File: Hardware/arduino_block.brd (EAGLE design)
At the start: 30.5 x 62.2 mm, 39 parts, among them U1 MIC5205-3.3V (150mA), U2 EDISON_CONNECTOR_FULLMOUNTING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, U3 EDISON_CONNECTOR_FULLHEADER, U4 ATMEGA328, Y1 8MHZ

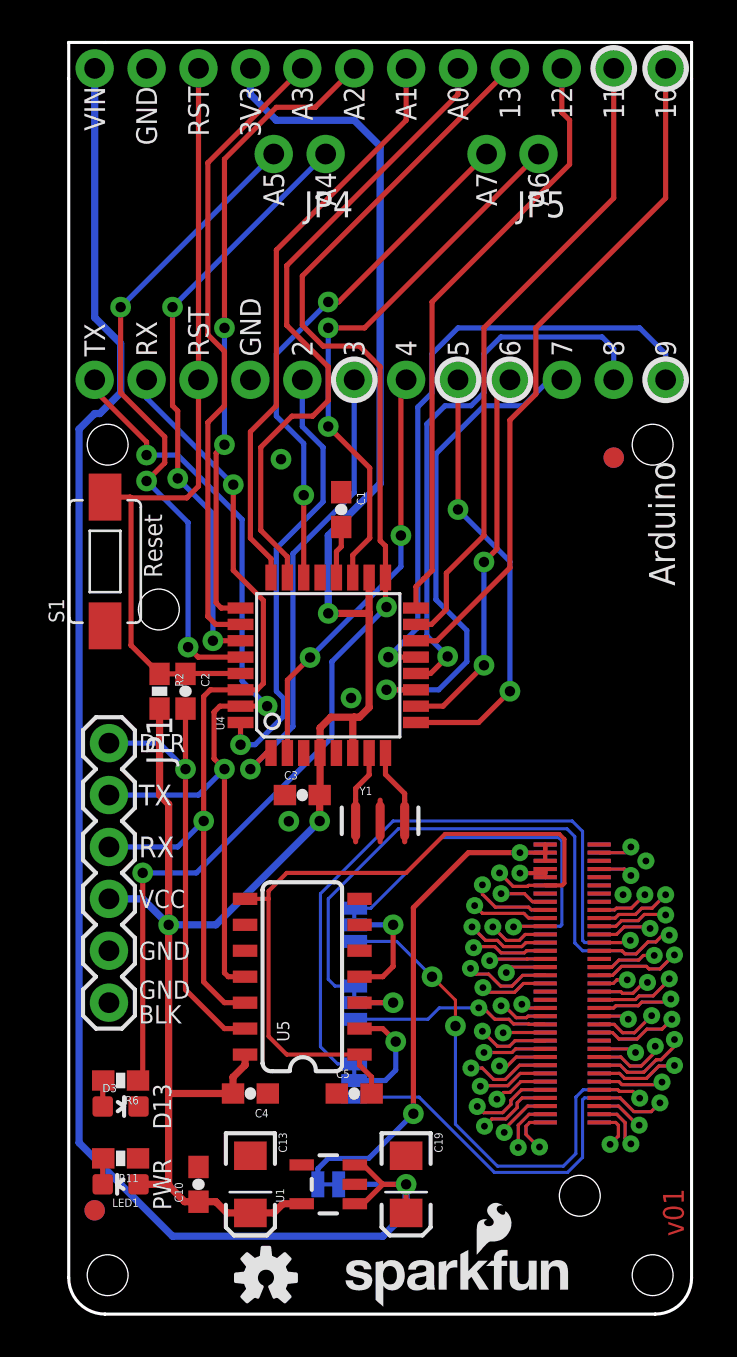
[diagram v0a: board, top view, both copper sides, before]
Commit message: Swapping jumpers to default to UART 1. Updating silk. (v02)
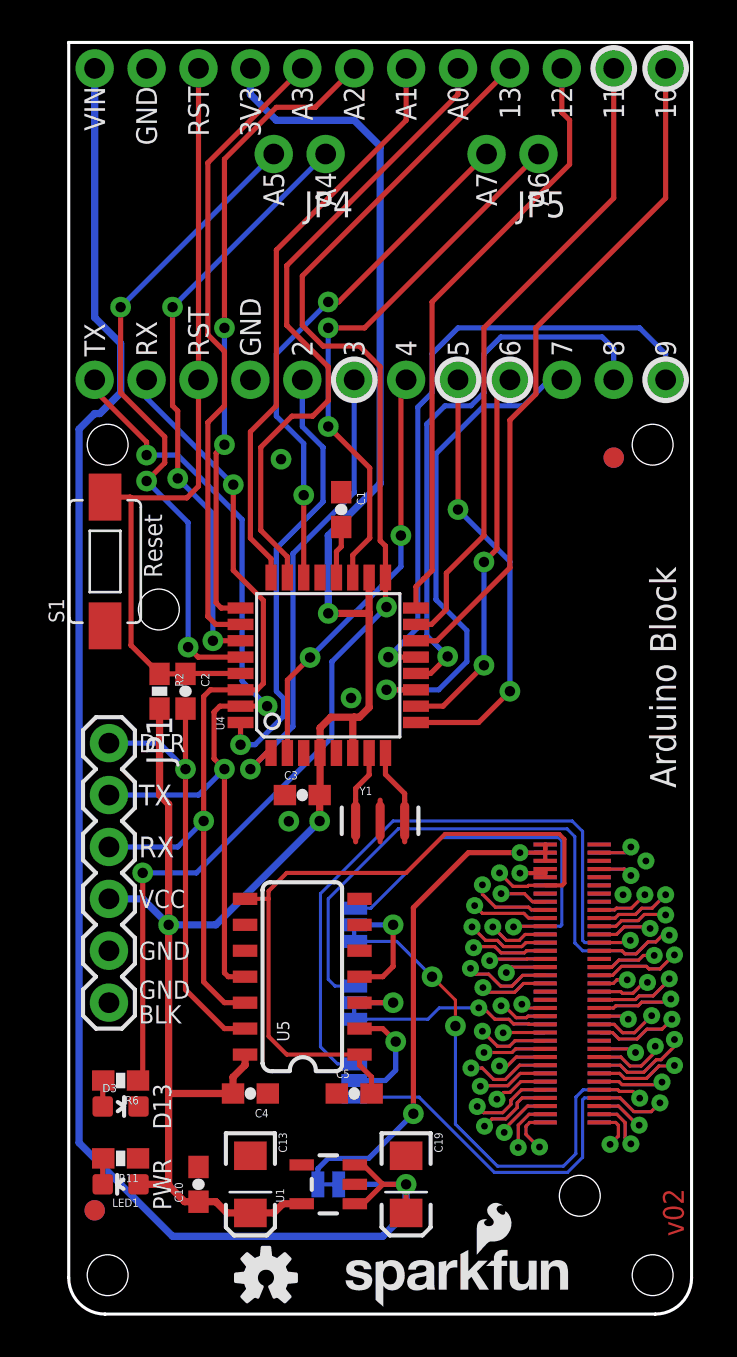
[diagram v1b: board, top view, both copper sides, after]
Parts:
- turned SJ1 to 270 degrees
- turned SJ2 to 270 degrees
- turned SJ3 to 270 degrees
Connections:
- net GP129_UART_1_RTS: now also SJ3.3; no longer SJ3.1
- net GP130_UART_1_RX: now also SJ2.3; no longer SJ2.1
- net GP131_UART_1_TX: now also SJ1.3; no longer SJ1.1
- net GP134_UART_2_RX: now also SJ2.1; no longer SJ2.3
- net GP135_UART_2_TX: now also SJ1.1; no longer SJ1.3
- net GP165: now also SJ3.1; no longer SJ3.3
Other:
- outline, holes or cut-outs redrawn
- board text added: "Arduino Block"
- board text added: "v02"
- board text removed: "Arduino"
- board text removed: "v01"
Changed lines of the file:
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@@
 <board>
 <plain>
-<wire x1="30.48" y1="60.452" x2="30.48" y2="1.778" width="0.1524" layer="20"/>
+<wire x1="30.48" y1="62.23" x2="30.48" y2="1.778" width="0.1524" layer="20"/>
 <wire x1="28.702" y1="0" x2="1.778" y2="0" width="0.1524" layer="20"/>
-<wire x1="0" y1="1.778" x2="0" y2="60.452" width="0.1524" layer="20"/>
+<wire x1="0" y1="1.778" x2="0" y2="62.23" width="0.1524" layer="20"/>
 <text x="25.4" y="-13.97" size="1.6764" layer="51" ratio="15">Jim Lindblom</text>
 <hole x="28.575" y="1.905" drill="2"/>
@@
 <hole x="1.905" y="42.545" drill="2"/>
 <hole x="28.575" y="42.545" drill="2"/>
-<text x="28.3972" y="41.7322" size="1.27" layer="21" font="vector" ratio="15" rot="R90" align="top-right">Arduino </text>
-<wire x1="1.778" y1="62.23" x2="28.702" y2="62.23" width="0.1524" layer="20"/>
+<text x="29.718" y="25.74798125" size="1.27" layer="21" font="vector" ratio="15" rot="R90">Arduino Block</text>
+<wire x1="0" y1="62.23" x2="30.48" y2="62.23" width="0.1524" layer="20"/>
 <wire x1="30.48" y1="1.778" x2="28.702" y2="0" width="0.1524" layer="20" curve="-90"/>
 <wire x1="1.778" y1="0" x2="0" y2="1.778" width="0.1524" layer="20" curve="-90"/>
-<wire x1="0" y1="60.452" x2="0" y2="62.23" width="0.1524" layer="20"/>
-<wire x1="0" y1="62.23" x2="1.778" y2="62.23" width="0.1524" layer="20"/>
-<wire x1="28.702" y1="62.23" x2="30.48" y2="62.23" width="0.1524" layer="20"/>
-<wire x1="30.48" y1="62.23" x2="30.48" y2="60.452" width="0.1524" layer="20"/>
 <rectangle x1="22.098" y1="26.162" x2="30.48" y2="44.45" layer="42" rot="R180"/>
 <rectangle x1="22.098" y1="26.162" x2="30.48" y2="44.45" layer="41" rot="R180"/>
 <text x="29.21" y="6.35" size="1.016" layer="22" font="vector" ratio="15" rot="MR90" align="center">4xM2.0</text>
-<text x="30.099" y="3.81" size="1.016" layer="1" font="vector" ratio="14" rot="R90">v01</text>
+<text x="30.099" y="3.81" size="1.016" layer="1" font="vector" ratio="14" rot="R90">v02</text>
 <text x="3.429" y="27.94" size="0.889" layer="21" font="vector" ratio="15" align="center-left">DTR</text>
 <text x="3.429" y="25.4" size="1.016" layer="21" font="vector" ratio="15" align="center-left">TX</text>
@@
 <text x="20.447" y="55.88" size="1.016" layer="22" font="vector" ratio="15" rot="MR90" align="center-right">A7</text>
 <text x="22.987" y="55.88" size="1.016" layer="22" font="vector" ratio="15" rot="MR90" align="center-right">A6</text>
-<text x="29.5148" y="41.7322" size="1.27" layer="22" font="vector" ratio="15" rot="MR90" align="top-right">Arduino </text>
+<text x="29.718" y="40.005" size="1.27" layer="22" font="vector" ratio="15" rot="MR270">Arduino Block</text>
 </plain>
 <attributes>
@@
 <attribute name="PROD_ID" value="XTAL-08895" x="15.24" y="24.13" size="1.778" layer="27" font="vector" ratio="15" display="off"/>
 </element>
-<element name="SJ1" library="SparkFun-Passives" package="PAD-JUMPER-3-2OF3_NC_BY_TRACE_YES_SILK_FULL_BOX" value="TX" x="13.97" y="15.24" rot="MR90"/>
-<element name="SJ2" library="SparkFun-Passives" package="PAD-JUMPER-3-2OF3_NC_BY_TRACE_YES_SILK_FULL_BOX" value="RX" x="13.97" y="19.05" rot="MR90"/>
+<element name="SJ1" library="SparkFun-Passives" package="PAD-JUMPER-3-2OF3_NC_BY_TRACE_YES_SILK_FULL_BOX" value="TX" x="13.97" y="15.24" rot="MR270"/>
+<element name="SJ2" library="SparkFun-Passives" package="PAD-JUMPER-3-2OF3_NC_BY_TRACE_YES_SILK_FULL_BOX" value="RX" x="13.97" y="19.05" rot="MR270"/>
 <element name="SJ4" library="SparkFun-Passives" package="PAD-JUMPER-2-NC_BY_TRACE_YES_SILK" value="VIN" x="12.7" y="6.35" rot="MR180"/>
-<element name="SJ3" library="SparkFun-Passives" package="PAD-JUMPER-3-2OF3_NC_BY_TRACE_YES_SILK_FULL_BOX" value="TX" x="13.97" y="11.43" rot="MR90"/>
+<element name="SJ3" library="SparkFun-Passives" package="PAD-JUMPER-3-2OF3_NC_BY_TRACE_YES_SILK_FULL_BOX" value="TX" x="13.97" y="11.43" rot="MR270"/>
 <element name="U5" library="SparkFun-DigitalIC" package="SO14" value="" x="11.43" y="16.51" rot="R90">
 <attribute name="PROD_ID" value="IC-11329" x="11.43" y="16.51" size="1.778" layer="27" font="vector" ratio="15" rot="R90" display="off"/>
@@
 <contactref element="U2" pad="25"/>
 <contactref element="U3" pad="25"/>
-<contactref element="SJ3" pad="3"/>
 <wire x1="25.96" y1="18.18" x2="25.254" y2="18.18" width="0.1524" layer="16"/>
 <wire x1="25.254" y1="18.18" x2="25.146" y2="18.288" width="0.1524" layer="16"/>
@@
 <wire x1="25.146" y1="23.622" x2="24.638" y2="24.13" width="0.1524" layer="16"/>
 <wire x1="24.638" y1="24.13" x2="15.875" y2="24.13" width="0.1524" layer="16"/>
-<wire x1="13.97" y1="12.2428" x2="13.1572" y2="12.2428" width="0.1524" layer="16"/>
 <wire x1="13.1572" y1="12.2428" x2="12.319" y2="13.081" width="0.1524" layer="16"/>
 <wire x1="12.319" y1="13.081" x2="12.319" y2="20.574" width="0.1524" layer="16"/>
 <wire x1="12.319" y1="20.574" x2="15.875" y2="24.13" width="0.1524" layer="16"/>
+<contactref element="SJ3" pad="1"/>
+<wire x1="13.97" y1="12.2428" x2="13.1572" y2="12.2428" width="0.1524" layer="16"/>
 </signal>
 <signal name="GP44">
@@
 <contactref element="U2" pad="27"/>
 <contactref element="U3" pad="27"/>
-<contactref element="SJ1" pad="3"/>
 <wire x1="25.96" y1="17.78" x2="25.146" y2="17.78" width="0.1524" layer="16"/>
 <wire x1="25.146" y1="17.78" x2="24.765" y2="18.161" width="0.1524" layer="16"/>
@@
 <wire x1="12.7" y1="20.32" x2="12.7" y2="16.383" width="0.1524" layer="16"/>
 <wire x1="12.7" y1="16.383" x2="13.0302" y2="16.0528" width="0.1524" layer="16"/>
-<wire x1="13.97" y1="16.0528" x2="13.0302" y2="16.0528" width="0.1524" layer="16"/>
+<contactref element="SJ1" pad="1"/>
+<wire x1="13.0302" y1="16.0528" x2="13.97" y2="16.0528" width="0.1524" layer="16"/>
 </signal>
 <signal name="GP134_UART_2_RX">
@@
 <contactref element="U2" pad="22"/>
 <contactref element="U3" pad="22"/>
-<contactref element="SJ2" pad="3"/>
 <wire x1="23.32" y1="18.98" x2="24.06" y2="18.98" width="0.1524" layer="16"/>
 <wire x1="24.06" y1="18.98" x2="24.13" y2="19.05" width="0.1524" layer="16"/>
@@
 <wire x1="23.9776" y1="23.3172" x2="18.2372" y2="23.3172" width="0.1524" layer="16"/>
 <wire x1="18.2372" y1="23.3172" x2="14.7828" y2="19.8628" width="0.1524" layer="16"/>
-<wire x1="13.97" y1="19.8628" x2="14.7828" y2="19.8628" width="0.1524" layer="16"/>
+<contactref element="SJ2" pad="1"/>
+<wire x1="14.7828" y1="19.8628" x2="13.97" y2="19.8628" width="0.1524" layer="16"/>
 </signal>
 <signal name="GP43_I2S_2_TXD">
@@
 <contactref element="U2" pad="46"/>
 <contactref element="U3" pad="46"/>
-<contactref element="SJ1" pad="1"/>
 <wire x1="20.066" y1="14.986" x2="18.1356" y2="14.986" width="0.1524" layer="16"/>
 <wire x1="18.1356" y1="14.986" x2="17.5768" y2="14.4272" width="0.1524" layer="16"/>
-<wire x1="17.5768" y1="14.4272" x2="13.97" y2="14.4272" width="0.1524" layer="16"/>
+<contactref element="SJ1" pad="3"/>
+<wire x1="13.97" y1="14.4272" x2="17.5768" y2="14.4272" width="0.1524" layer="16"/>
 </signal>
 <signal name="GP130_UART_1_RX">
@@
 <contactref element="U2" pad="61"/>
 <contactref element="U3" pad="61"/>
-<contactref element="SJ2" pad="1"/>
 <wire x1="25.96" y1="10.98" x2="25.1786" y2="10.98" width="0.1524" layer="16"/>
 <wire x1="25.1786" y1="10.98" x2="24.8158" y2="10.6172" width="0.1524" layer="16"/>
@@
 <via x="17.78" y="16.51" extent="1-16" drill="0.508"/>
 <wire x1="17.78" y1="16.51" x2="16.0528" y2="18.2372" width="0.1524" layer="16"/>
-<wire x1="16.0528" y1="18.2372" x2="13.97" y2="18.2372" width="0.1524" layer="16"/>
+<contactref element="SJ2" pad="3"/>
+<wire x1="13.97" y1="18.2372" x2="16.0528" y2="18.2372" width="0.1524" layer="16"/>
 </signal>
 <signal name="GP129_UART_1_RTS">
@@
 <contactref element="U2" pad="63"/>
 <contactref element="U3" pad="63"/>
-<contactref element="SJ3" pad="1"/>
 <wire x1="25.96" y1="10.58" x2="25.2358" y2="10.58" width="0.1524" layer="16"/>
 <wire x1="25.2358" y1="10.58" x2="25.146" y2="10.4902" width="0.1524" layer="16"/>
@@
 <wire x1="25.146" y1="7.6708" x2="24.4094" y2="6.9342" width="0.1524" layer="16"/>
 <wire x1="24.4094" y1="6.9342" x2="20.828" y2="6.9342" width="0.1524" layer="16"/>
+<wire x1="17.145" y1="10.6172" x2="20.828" y2="6.9342" width="0.1524" layer="16"/>
+<contactref element="SJ3" pad="3"/>
 <wire x1="13.97" y1="10.6172" x2="17.145" y2="10.6172" width="0.1524" layer="16"/>
-<wire x1="17.145" y1="10.6172" x2="20.828" y2="6.9342" width="0.1524" layer="16"/>
 </signal>
 <signal name="GP128_UART_1_CTS">

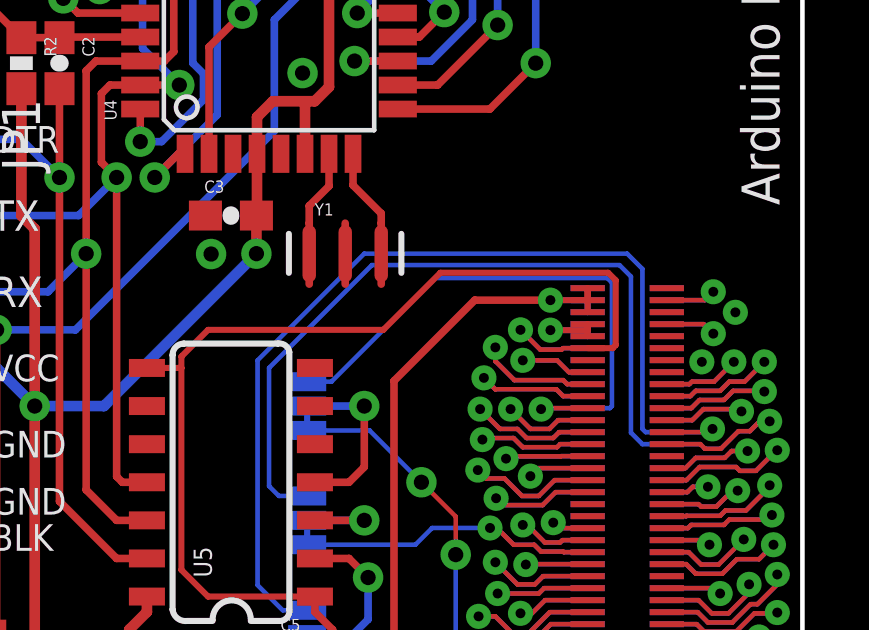
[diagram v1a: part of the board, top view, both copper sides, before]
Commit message: Stacking DCIN through. Adding jumper to potentially connect it to VSYS
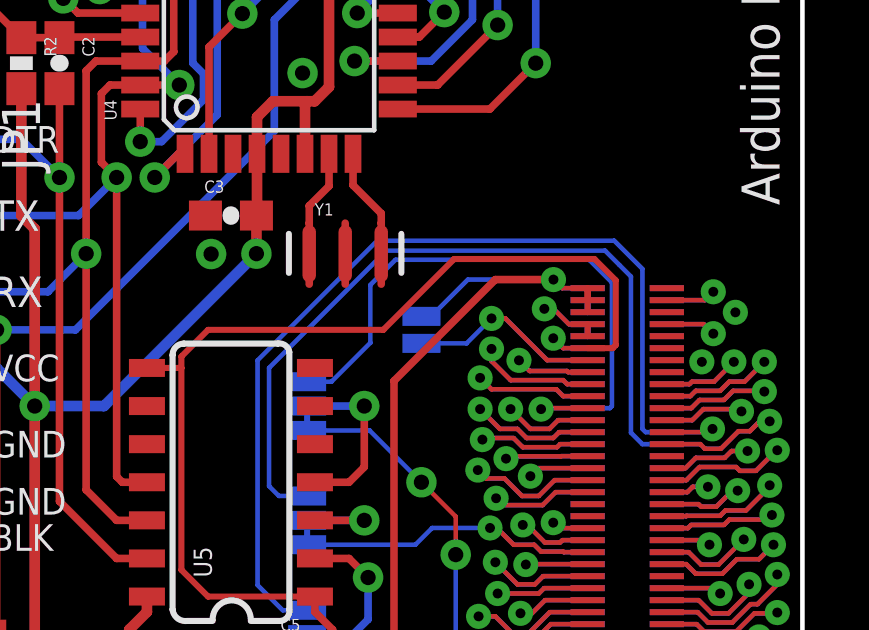
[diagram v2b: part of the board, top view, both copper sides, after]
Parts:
- added SJ5: DCIN, SparkFun-Passives:PAD-JUMPER-2-NO_YES_SILK
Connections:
- new net DCIN: SJ5.1, U2.14, U3.14
- net VSYS: now also SJ5.2
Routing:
- net DCIN: track 0.00 -> 10.2 mm, vias 0 -> 1
- net VSYS: track 27.4 -> 32.8 mm
- net 1.8V: track 39.2 -> 37.1 mm
- net GP134_UART_2_RX: track 19.7 -> 21.4 mm
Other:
- board text added: "DCIN"
- board text added: "VSYS"
